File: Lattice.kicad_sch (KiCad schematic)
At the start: 108 parts, among them J1 Conn_01x10_Male, J2 Conn_01x10_Female, J3 Conn_01x10_Male, J4 Conn_01x10_Female, J5 clock_out, J6 any trig, J7 midi in, J8 Synth_power_2x5, Q1 2N3904, Q2 2N3904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

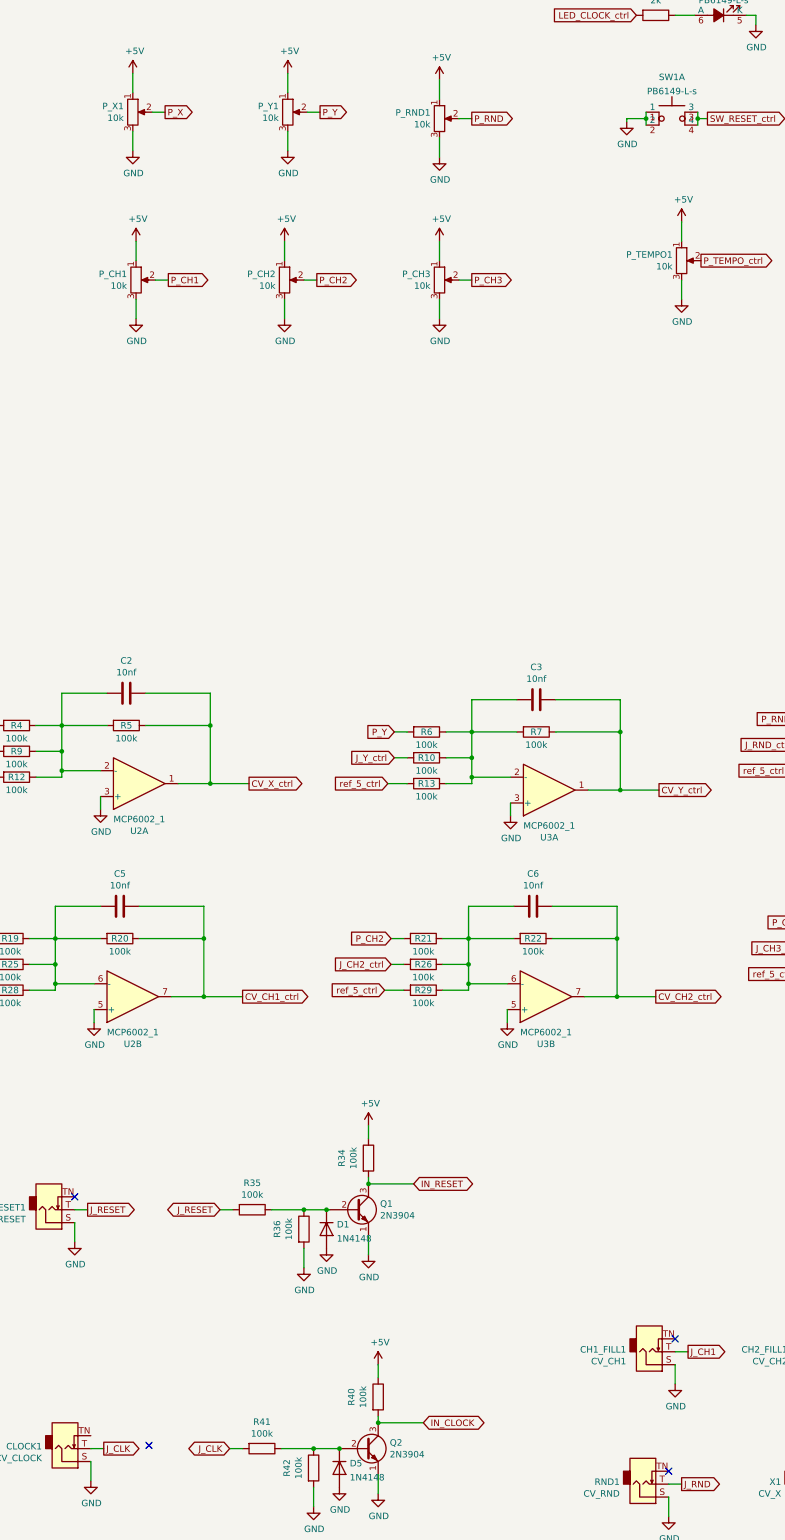
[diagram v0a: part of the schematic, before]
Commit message: fix pot direction
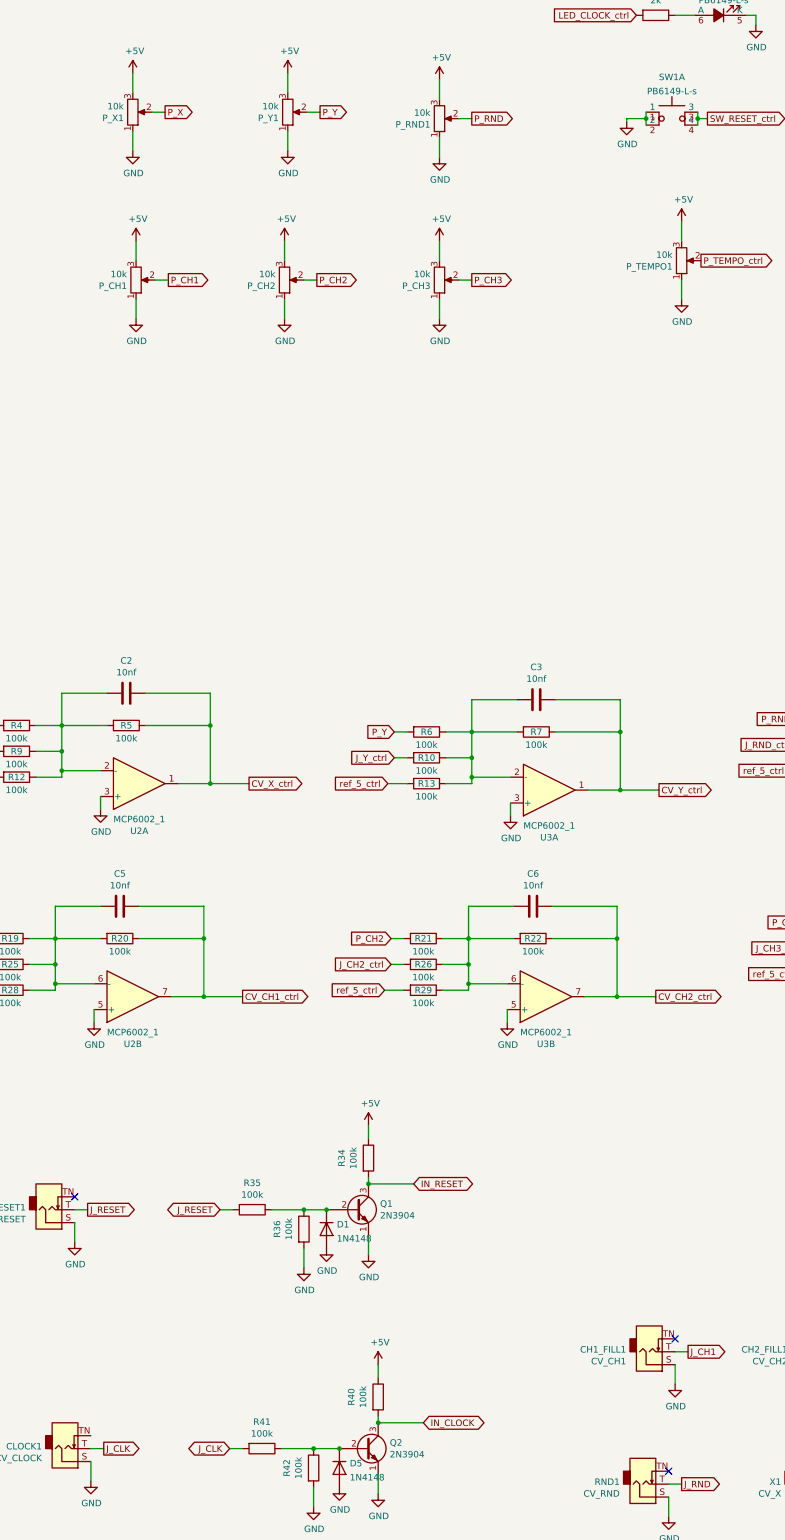
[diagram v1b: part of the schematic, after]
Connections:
- net +5V: now also P_CH1.3, P_CH2.3, P_CH3.3, P_RND1.3, P_TEMPO1.3, P_X1.3, P_Y1.3; no longer P_CH1.1, P_CH2.1, P_CH3.1, P_RND1.1, P_TEMPO1.1, P_X1.1, P_Y1.1
- net GND: now also P_CH1.1, P_CH2.1, P_CH3.1, P_RND1.1, P_TEMPO1.1, P_X1.1, P_Y1.1; no longer P_CH1.3, P_CH2.3, P_CH3.3, P_RND1.3, P_TEMPO1.3, P_X1.3, P_Y1.3
- no-connect marks 25 -> 24
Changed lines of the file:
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@@
   (no_connect (at 167.005 309.88))
   (no_connect (at 50.165 255.905))
-  (no_connect (at 64.77 304.8))
   (no_connect (at 403.86 246.38))
   (no_connect (at 403.86 276.86))
@@
     (pin "TN")
   )
-  (symbol (lib_id "NanoGris-rescue:R_POT-Device-GridsNanoV3-rescue") (at 92.075 42.545 0) (unit 1)
+  (symbol (lib_id "NanoGris-rescue:R_POT-Device-GridsNanoV3-rescue") (at 92.075 42.545 0) (mirror x) (unit 1)
     (in_bom yes) (on_board yes)
-    (property "Reference" "P_Y1" (id 0) (at 90.297 41.3766 0)
+    (property "Reference" "P_Y1" (id 0) (at 90.297 43.7134 0)
       (effects (font (size 1.27 1.27)) (justify right))
     )
-    (property "Value" "10k" (id 1) (at 90.297 43.688 0)
+    (property "Value" "10k" (id 1) (at 90.297 41.402 0)
       (effects (font (size 1.27 1.27)) (justify right))
     )
@@
     (pin "TN")
   )
-  (symbol (lib_id "NanoGris-rescue:R_POT-Device-GridsNanoV3-rescue") (at 61.595 42.545 0) (unit 1)
+  (symbol (lib_id "NanoGris-rescue:R_POT-Device-GridsNanoV3-rescue") (at 61.595 42.545 0) (mirror x) (unit 1)
     (in_bom yes) (on_board yes)
-    (property "Reference" "P_X1" (id 0) (at 59.817 41.3766 0)
+    (property "Reference" "P_X1" (id 0) (at 59.817 43.7134 0)
       (effects (font (size 1.27 1.27)) (justify right))
     )
-    (property "Value" "10k" (id 1) (at 59.817 43.688 0)
+    (property "Value" "10k" (id 1) (at 59.817 41.402 0)
       (effects (font (size 1.27 1.27)) (justify right))
     )
@@
     (pin "1")
   )
-  (symbol (lib_id "NanoGris-rescue:R_POT-Device-GridsNanoV3-rescue") (at 62.23 75.565 0) (unit 1)
+  (symbol (lib_id "NanoGris-rescue:R_POT-Device-GridsNanoV3-rescue") (at 62.23 75.565 0) (mirror x) (unit 1)
     (in_bom yes) (on_board yes)
-    (property "Reference" "P_CH1" (id 0) (at 60.452 74.3966 0)
+    (property "Reference" "P_CH1" (id 0) (at 60.452 76.7334 0)
       (effects (font (size 1.27 1.27)) (justify right))
     )
-    (property "Value" "10k" (id 1) (at 60.452 76.708 0)
+    (property "Value" "10k" (id 1) (at 60.452 74.422 0)
       (effects (font (size 1.27 1.27)) (justify right))
     )
@@
     (pin "TN")
   )
-  (symbol (lib_id "NanoGris-rescue:R_POT-Device-GridsNanoV3-rescue") (at 91.44 75.565 0) (unit 1)
+  (symbol (lib_id "NanoGris-rescue:R_POT-Device-GridsNanoV3-rescue") (at 91.44 75.565 0) (mirror x) (unit 1)
     (in_bom yes) (on_board yes)
-    (property "Reference" "P_CH2" (id 0) (at 89.662 74.3966 0)
+    (property "Reference" "P_CH2" (id 0) (at 89.662 76.7334 0)
       (effects (font (size 1.27 1.27)) (justify right))
     )
-    (property "Value" "10k" (id 1) (at 89.662 76.708 0)
+    (property "Value" "10k" (id 1) (at 89.662 74.422 0)
       (effects (font (size 1.27 1.27)) (justify right))
     )
@@
     (pin "TN")
   )
-  (symbol (lib_id "NanoGris-rescue:R_POT-Device-GridsNanoV3-rescue") (at 121.92 43.815 0) (unit 1)
+  (symbol (lib_id "NanoGris-rescue:R_POT-Device-GridsNanoV3-rescue") (at 121.92 43.815 0) (mirror x) (unit 1)
     (in_bom yes) (on_board yes)
-    (property "Reference" "P_RND1" (id 0) (at 120.142 42.6466 0)
+    (property "Reference" "P_RND1" (id 0) (at 120.142 44.9834 0)
       (effects (font (size 1.27 1.27)) (justify right))
     )
-    (property "Value" "10k" (id 1) (at 120.142 44.958 0)
+    (property "Value" "10k" (id 1) (at 120.142 42.672 0)
       (effects (font (size 1.27 1.27)) (justify right))
     )
@@
     (pin "TN")
   )
-  (symbol (lib_id "NanoGris-rescue:R_POT-Device-GridsNanoV3-rescue") (at 121.92 75.565 0) (unit 1)
+  (symbol (lib_id "NanoGris-rescue:R_POT-Device-GridsNanoV3-rescue") (at 121.92 75.565 0) (mirror x) (unit 1)
     (in_bom yes) (on_board yes)
-    (property "Reference" "P_CH3" (id 0) (at 120.142 74.3966 0)
+    (property "Reference" "P_CH3" (id 0) (at 120.142 76.7334 0)
       (effects (font (size 1.27 1.27)) (justify right))
     )
-    (property "Value" "10k" (id 1) (at 120.142 76.708 0)
+    (property "Value" "10k" (id 1) (at 120.142 74.422 0)
       (effects (font (size 1.27 1.27)) (justify right))
     )
@@
     (pin "TN")
   )
-  (symbol (lib_id "NanoGris-rescue:R_POT-Device-GridsNanoV3-rescue") (at 169.545 71.755 0) (unit 1)
+  (symbol (lib_id "NanoGris-rescue:R_POT-Device-GridsNanoV3-rescue") (at 169.545 71.755 0) (mirror x) (unit 1)
     (in_bom yes) (on_board yes)
-    (property "Reference" "P_TEMPO1" (id 0) (at 167.767 70.5866 0)
+    (property "Reference" "P_TEMPO1" (id 0) (at 167.767 72.9234 0)
       (effects (font (size 1.27 1.27)) (justify right))
     )
-    (property "Value" "10k" (id 1) (at 167.767 72.898 0)
+    (property "Value" "10k" (id 1) (at 167.767 70.612 0)
       (effects (font (size 1.27 1.27)) (justify right))
     )

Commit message: fix button
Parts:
- R37, R38, R39: value 100r -> 2.2k
- SW1: symbol sebi_symbols:PB6149-L-s -> sebikicadparts:SW_Push_LED
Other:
- note added: "adjust resistors depending on led"
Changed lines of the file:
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@@
     (stroke (width 0) (type default) (color 0 0 0 0))
   )
+  (text "adjust resistors \ndepending on led" (at 523.24 261.62 0)
+    (effects (font (size 1.27 1.27)) (justify left bottom))
+  )
   (global_label "IN_CLOCK" (shape bidirectional) (at 118.745 300.355 0) (fields_autoplaced)
     (effects (font (size 1.27 1.27)) (justify left))
@@
     (pin "2")
     (pin "3")
+    (pin "5")
+    (pin "6")
+    (pin "7")
+    (pin "4")
+    (pin "8")
   )
   (symbol (lib_id "NanoGris-rescue:MCP6002-xP-Amplifier_Operational-GridsNanoV3-rescue") (at 61.595 216.535 0) (mirror x) (unit 2)
@@
       (effects (font (size 1.27 1.27)) hide)
     )
+    (pin "1")
+    (pin "2")
+    (pin "3")
     (pin "5")
     (pin "6")
     (pin "7")
+    (pin "4")
+    (pin "8")
   )
   (symbol (lib_id "NanoGris-rescue:MCP6002-xP-Amplifier_Operational-GridsNanoV3-rescue") (at 243.84 382.905 0) (unit 3)
@@
       (effects (font (size 1.27 1.27)) hide)
     )
+    (pin "1")
+    (pin "2")
+    (pin "3")
+    (pin "5")
+    (pin "6")
+    (pin "7")
     (pin "4")
     (pin "8")
@@
       (effects (font (size 1.27 1.27)) hide)
     )
+    (pin "1")
+    (pin "2")
+    (pin "3")
+    (pin "5")
+    (pin "6")
+    (pin "7")
     (pin "4")
     (pin "8")
@@
       (effects (font (size 1.27 1.27)) hide)
     )
+    (pin "1")
+    (pin "2")
+    (pin "3")
     (pin "5")
     (pin "6")
     (pin "7")
+    (pin "4")
+    (pin "8")
   )
   (symbol (lib_id "NanoGris-rescue:MCP6002-xP-Amplifier_Operational-GridsNanoV3-rescue") (at 143.51 175.895 0) (mirror x) (unit 1)
@@
     (pin "2")
     (pin "3")
+    (pin "5")
+    (pin "6")
+    (pin "7")
+    (pin "4")
+    (pin "8")
   )
   (symbol (lib_id "NanoGris-rescue:GND-power-GridsNanoV3-rescue") (at 53.975 221.615 0) (unit 1)
@@
       (effects (font (size 1.27 1.27)) hide)
     )
+    (pin "1")
+    (pin "2")
+    (pin "3")
+    (pin "5")
+    (pin "6")
+    (pin "7")
     (pin "4")
     (pin "8")
@@
       (effects (font (size 1.27 1.27)) hide)
     )
+    (pin "1")
+    (pin "2")
+    (pin "3")
     (pin "5")
     (pin "6")
     (pin "7")
+    (pin "4")
+    (pin "8")
   )
   (symbol (lib_id "NanoGris-rescue:MCP6002-xP-Amplifier_Operational-GridsNanoV3-rescue") (at 222.885 173.355 0) (mirror x) (unit 1)
@@
     (pin "2")
     (pin "3")
+    (pin "5")
+    (pin "6")
+    (pin "7")
+    (pin "4")
+    (pin "8")
   )
   (symbol (lib_id "NanoGris-rescue:GND-power-GridsNanoV3-rescue") (at 217.17 218.44 0) (unit 1)
@@
     (in_bom yes) (on_board yes)
     (property "Reference" "R39" (id 0) (at 532.765 282.3972 90))
-    (property "Value" "100r" (id 1) (at 532.765 284.7086 90))
+    (property "Value" "2.2k" (id 1) (at 532.765 284.7086 90))
     (property "Footprint" "ao_tht:R_Axial_DIN0207_L6.3mm_D2.5mm_P10.16mm_Horizontal" (id 2) (at 532.765 285.877 90)
       (effects (font (size 1.27 1.27)) hide)
@@
     (pin "2")
   )
-  (symbol (lib_id "NanoGris-rescue:R-Device-GridsNanoV3-rescue") (at 532.765 278.765 270) (unit 1)
-    (in_bom yes) (on_board yes)
-    (property "Reference" "R38" (id 0) (at 532.765 273.5072 90))
-    (property "Value" "100r" (id 1) (at 532.765 275.8186 90))
-    (property "Footprint" "ao_tht:R_Axial_DIN0207_L6.3mm_D2.5mm_P10.16mm_Horizontal" (id 2) (at 532.765 276.987 90)
-      (effects (font (size 1.27 1.27)) hide)
-    )
-    (property "Datasheet" "~" (id 3) (at 532.765 278.765 0)
-      (effects (font (size 1.27 1.27)) hide)
-    )
-    (pin "1")
-    (pin "2")
-  )
   (symbol (lib_id "NanoGris-rescue:R-Device-GridsNanoV3-rescue") (at 532.765 269.875 270) (unit 1)
     (in_bom yes) (on_board yes)
     (property "Reference" "R37" (id 0) (at 532.765 264.6172 90))
-    (property "Value" "100r" (id 1) (at 532.765 266.9286 90))
+    (property "Value" "2.2k" (id 1) (at 532.765 266.9286 90))
     (property "Footprint" "ao_tht:R_Axial_DIN0207_L6.3mm_D2.5mm_P10.16mm_Horizontal" (id 2) (at 532.765 268.097 90)
       (effects (font (size 1.27 1.27)) hide)
@@
     (pin "9")
   )
-  (symbol (lib_id "sebi_symbols:PB6149-L-s") (at 162.56 45.085 0) (unit 1)
+  (symbol (lib_id "sebikicadparts:SW_Push_LED") (at 162.56 45.085 0) (unit 1)
     (in_bom yes) (on_board yes) (fields_autoplaced)
     (property "Reference" "SW1" (id 0) (at 167.64 35.6575 0))
@@
     (pin "3")
     (pin "4")
+    (pin "5")
+    (pin "6")
   )
   (symbol (lib_id "Connector:Conn_01x10_Female") (at 262.89 43.815 0) (mirror y) (unit 1)
@@
     (pin "1")
   )
+  (symbol (lib_id "NanoGris-rescue:R-Device-GridsNanoV3-rescue") (at 532.765 278.765 270) (unit 1)
+    (in_bom yes) (on_board yes)
+    (property "Reference" "R38" (id 0) (at 532.765 273.5072 90))
+    (property "Value" "2.2k" (id 1) (at 532.765 275.8186 90))
+    (property "Footprint" "ao_tht:R_Axial_DIN0207_L6.3mm_D2.5mm_P10.16mm_Horizontal" (id 2) (at 532.765 276.987 90)
+      (effects (font (size 1.27 1.27)) hide)
+    )
+    (property "Datasheet" "~" (id 3) (at 532.765 278.765 0)
+      (effects (font (size 1.27 1.27)) hide)
+    )
+    (pin "1")
+    (pin "2")
+  )
   (symbol (lib_id "NanoGris-rescue:GND-power-GridsNanoV3-rescue") (at 474.98 266.065 0) (unit 1)
     (in_bom yes) (on_board yes)
@@
     (pin "1")
   )
-  (symbol (lib_id "sebi_symbols:PB6149-L-s") (at 182.245 23.495 180) (unit 2)
+  (symbol (lib_id "sebikicadparts:SW_Push_LED") (at 182.245 23.495 180) (unit 2)
     (in_bom yes) (on_board yes) (fields_autoplaced)
     (property "Reference" "SW1" (id 0) (at 177.8 17.7505 0))
@@
       (effects (font (size 1.27 1.27)) hide)
     )
+    (pin "1")
+    (pin "2")
+    (pin "3")
+    (pin "4")
     (pin "5")
     (pin "6")
@@
     )
     (path "/00000000-0000-0000-0000-00005e4f940a"
-      (reference "R37") (unit 1) (value "100r") (footprint "ao_tht:R_Axial_DIN0207_L6.3mm_D2.5mm_P10.16mm_Horizontal")
+      (reference "R37") (unit 1) (value "2.2k") (footprint "ao_tht:R_Axial_DIN0207_L6.3mm_D2.5mm_P10.16mm_Horizontal")
     )
-    (path "/00000000-0000-0000-0000-00005e4f9404"
-      (reference "R38") (unit 1) (value "100r") (footprint "ao_tht:R_Axial_DIN0207_L6.3mm_D2.5mm_P10.16mm_Horizontal")
+    (path "/8ccc26b3-3f84-4ac5-b683-144073576eef"
+      (reference "R38") (unit 1) (value "2.2k") (footprint "ao_tht:R_Axial_DIN0207_L6.3mm_D2.5mm_P10.16mm_Horizontal")
     )
     (path "/00000000-0000-0000-0000-00005e4f93fe"
-      (reference "R39") (unit 1) (value "100r") (footprint "ao_tht:R_Axial_DIN0207_L6.3mm_D2.5mm_P10.16mm_Horizontal")
+      (reference "R39") (unit 1) (value "2.2k") (footprint "ao_tht:R_Axial_DIN0207_L6.3mm_D2.5mm_P10.16mm_Horizontal")
     )
     (path "/00000000-0000-0000-0000-00005e54ccc8"
